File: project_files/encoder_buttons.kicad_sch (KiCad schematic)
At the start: 36 parts, among them J1 Conn_01x08, J2 Conn_01x08, SW1 A, SW2 EC11, SW3 C, SW5 E, U1 74HC14

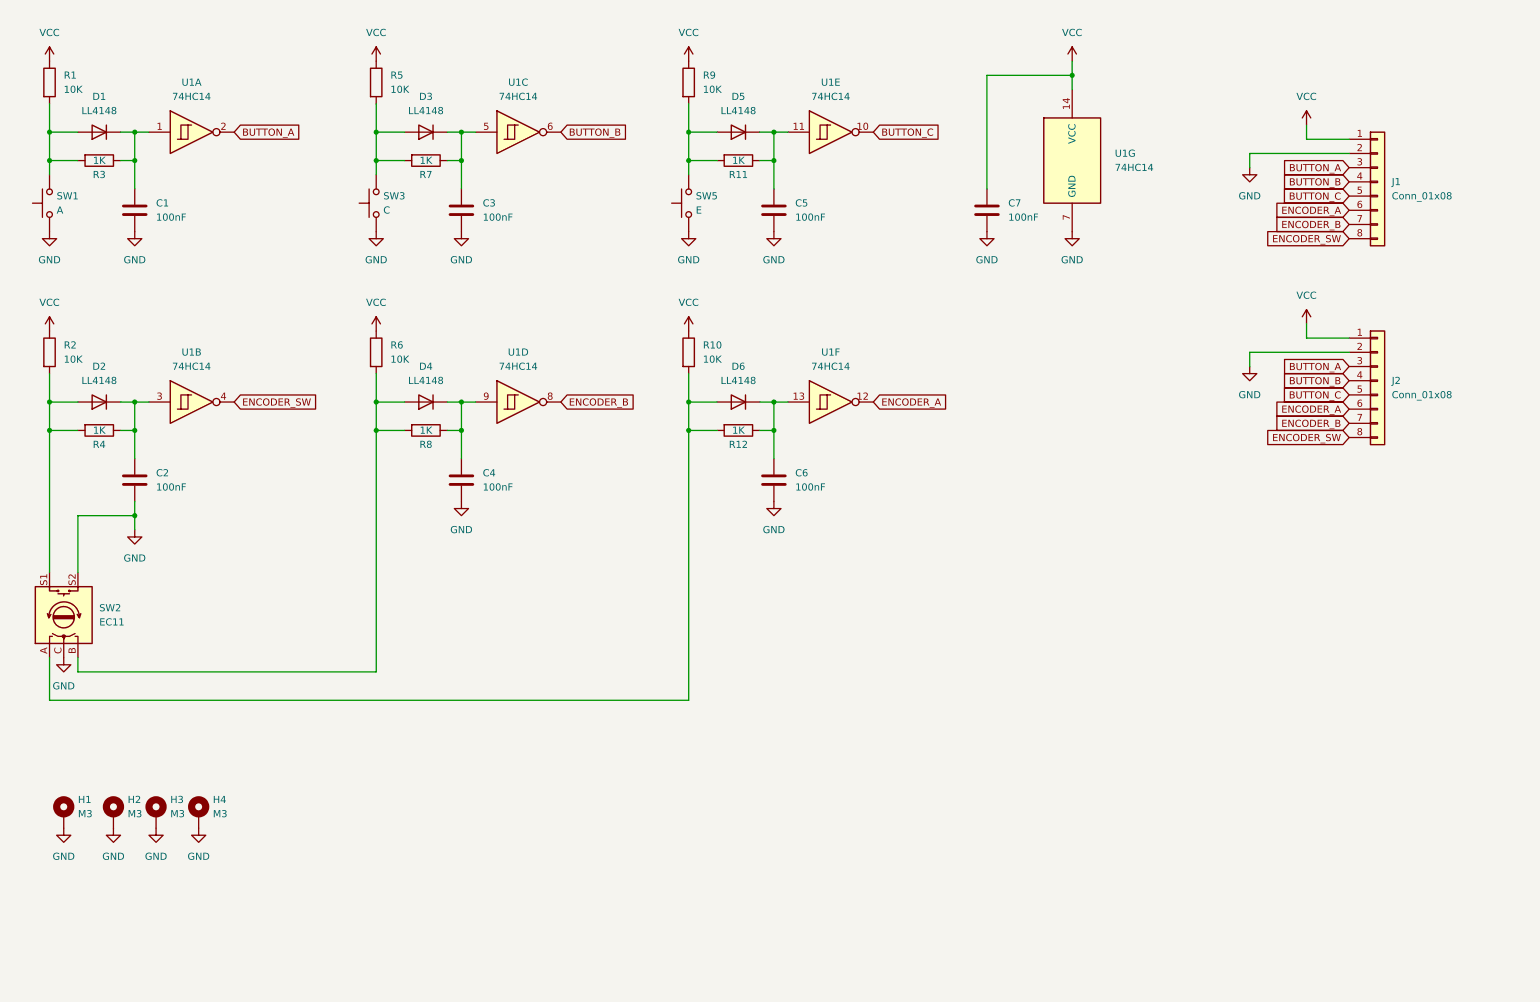
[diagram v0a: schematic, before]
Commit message: Reopened in Kicad 8
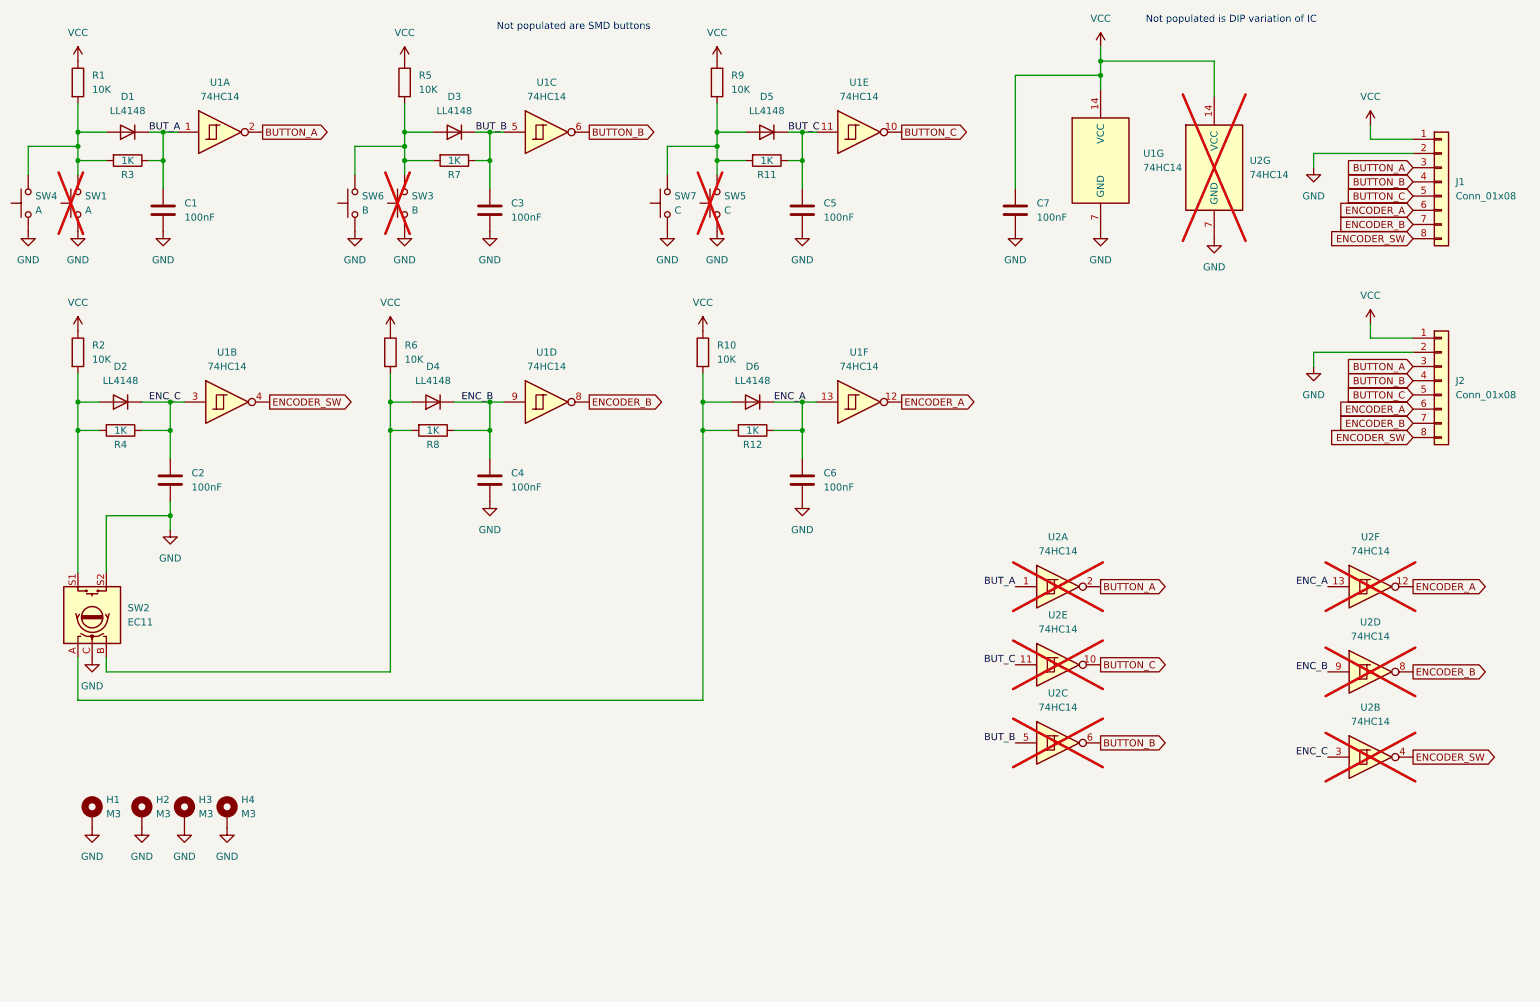
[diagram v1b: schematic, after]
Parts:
- added SW4: A, Button_Switch_THT:SW_PUSH_6mm, symbol Switch:SW_Push
- added SW6: B, Button_Switch_THT:SW_PUSH_6mm, symbol Switch:SW_Push
- added SW7: C, Button_Switch_THT:SW_PUSH_6mm, symbol Switch:SW_Push
- added U2: 74HC14, Package_DIP:DIP-14_W7.62mm, symbol 74xx:74HC14
- SW1: now not fitted
- SW3: value C -> B; now not fitted
- SW5: value E -> C; now not fitted
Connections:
- net BUTTON_A: now also U2.2
- net BUTTON_B: now also U2.6
- net BUTTON_C: now also U2.10
- net ENCODER_A: now also U2.12
- net ENCODER_B: now also U2.8
- net ENCODER_SW: now also U2.4
- net GND: now also SW4.1, SW6.1, SW7.1, U2.7 (GND)
- net VCC: now also U2.14 (VCC)
- net BUT_B: now reaches C3.1, D3.1 (K), R7.1, U1.5
- net BUT_B: now also U2.5
- net at D3.2 (A), R5.2, R7.2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: now also SW6.2
- net ENC_A: now reaches C6.1, D6.1 (K), R12.1, U1.13
- net ENC_A: now also U2.13
- net BUT_A: now reaches C1.1, D1.1 (K), R3.1, U1.1
- net BUT_A: now also U2.1
- net ENC_C: now reaches C2.1, D2.1 (K), R4.1, U1.3
- net ENC_C: now also U2.3
- net at D5.2 (A), R11.2, R9.2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: now also SW7.2
- net ENC_B: now reaches C4.1, D4.1 (K), R8.1, U1.9
- net ENC_B: now also U2.9
- net at D1.2 (A), R1.2, R3.2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: now also SW4.2
- net BUT_C: now reaches C5.1, D5.1 (K), R11.1, U1.11
- net BUT_C: now also U2.11
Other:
- note added: "Not populated are SMD buttons"
- note added: "Not populated is DIP variation of IC"
- moved on the sheet: C1, C2, C3, C4, C5, C6, C7, D1, D2, D3, D4, D5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

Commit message: placing the components
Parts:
- removed J2: Conn_01x08, Connector_PinHeader_2.54mm:PinHeader_1x08_P2.54mm_Vertical, symbol Connector_Generic:Conn_01x08
- removed SW2: EC11, Rotary_Encoder:RotaryEncoder_Alps_EC11E-Switch_Vertical_H20mm, symbol Device:RotaryEncoder_Switch
- added SW8: EC11, Rotary_Encoder:RotaryEncoder_Alps_EC11E-Switch_Vertical_H20mm, symbol Device:RotaryEncoder_Switch_MP
- J1: value Conn_01x08 -> UPPER
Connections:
- net BUTTON_B: now also U1.4, U2.4; no longer U1.6, U2.6
- net BUTTON_C: now also U1.6, U2.6; no longer U1.10, U2.10
- net BUT_B: now also U1.3, U2.3; no longer U1.5, U2.5
- net BUT_C: now also U1.5, U2.5; no longer U1.11, U2.11
- net ENCODER_B: now also U1.10, U2.10; no longer U1.8, U2.8
- net ENCODER_SW: now also U1.8, U2.8; no longer U1.4, U2.4
- net ENC_B: now also U1.11, U2.11; no longer U1.9, U2.9
- net ENC_C: now also U1.9, U2.9; no longer U1.3, U2.3
- net GND: now also SW8.C, SW8.MP, SW8.S2
- net at D2.2 (A), R2.2, R4.2: now also SW8.S1
- net at D6.2 (A), R10.2, R12.2: now also SW8.A
- net at D4.2 (A), R6.2, R8.2: now also SW8.B
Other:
- title: (none) -> Encoder and push-buttons module with hardware debouncing
- moved on the sheet: U1B, U1C, U1D, U1E, U2A, U2B, U2C, U2D, U2E, U2F, U2G

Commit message: Finalized and rendered
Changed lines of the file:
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@@
 	(text "Not populated is DIP variation of IC"
 		(exclude_from_sim no)
-		(at 232.918 18.034 0)
+		(at 233.68 113.03 0)
 		(effects
 			(font
@@
 					(unit 1)
 				)
+			)
+		)
+	)
+	(symbol
+		(lib_id "Graphic:Logo_Open_Hardware_Large")
+		(at 160.02 182.88 0)
+		(unit 1)
+		(exclude_from_sim no)
+		(in_bom no)
+		(on_board no)
+		(dnp no)
+		(fields_autoplaced yes)
+		(property "Reference" "#SYM1"
+			(at 160.02 170.18 0)
+			(effects
+				(font
+					(size 1.27 1.27)
+				)
+				(hide yes)
+			)
+		)
+		(property "Value" "Logo_Open_Hardware_Large"
+			(at 160.02 193.04 0)
+			(effects
+				(font
+					(size 1.27 1.27)
+				)
+				(hide yes)
+			)
+		)
+		(property "Footprint" ""
+			(at 160.02 182.88 0)
+			(effects
+				(font
+					(size 1.27 1.27)
+				)
+				(hide yes)
+			)
+		)
+		(property "Datasheet" "~"
+			(at 160.02 182.88 0)
+			(effects
+				(font
+					(size 1.27 1.27)
+				)
+				(hide yes)
+			)
+		)
+		(property "Description" "Open Hardware logo, large"
+			(at 160.02 182.88 0)
+			(effects
+				(font
+					(size 1.27 1.27)
+				)
+				(hide yes)
+			)
+		)
+		(property "Sim.Enable" "0"
+			(at 160.02 182.88 0)
+			(effects
+				(font
+					(size 1.27 1.27)
+				)
+				(hide yes)
+			)
+		)
+		(instances
+			(project "encoder_buttons"
+				(path "/bd410bad-7064-4a0d-9cb7-e928407f3c66"
+					(reference "#SYM1")
+					(unit 1)
+				)
